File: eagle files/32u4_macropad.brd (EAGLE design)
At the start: 75.2 x 98.6 mm, 89 parts, among them IC1 IS31FL3733-TQLS4, J1 TYPE-C-31-M-12, Q1 16Mhz, SW2 SWITCH-SMD-EVP-BB2A9B00, U1 ATMEGA32U4-TQFP44

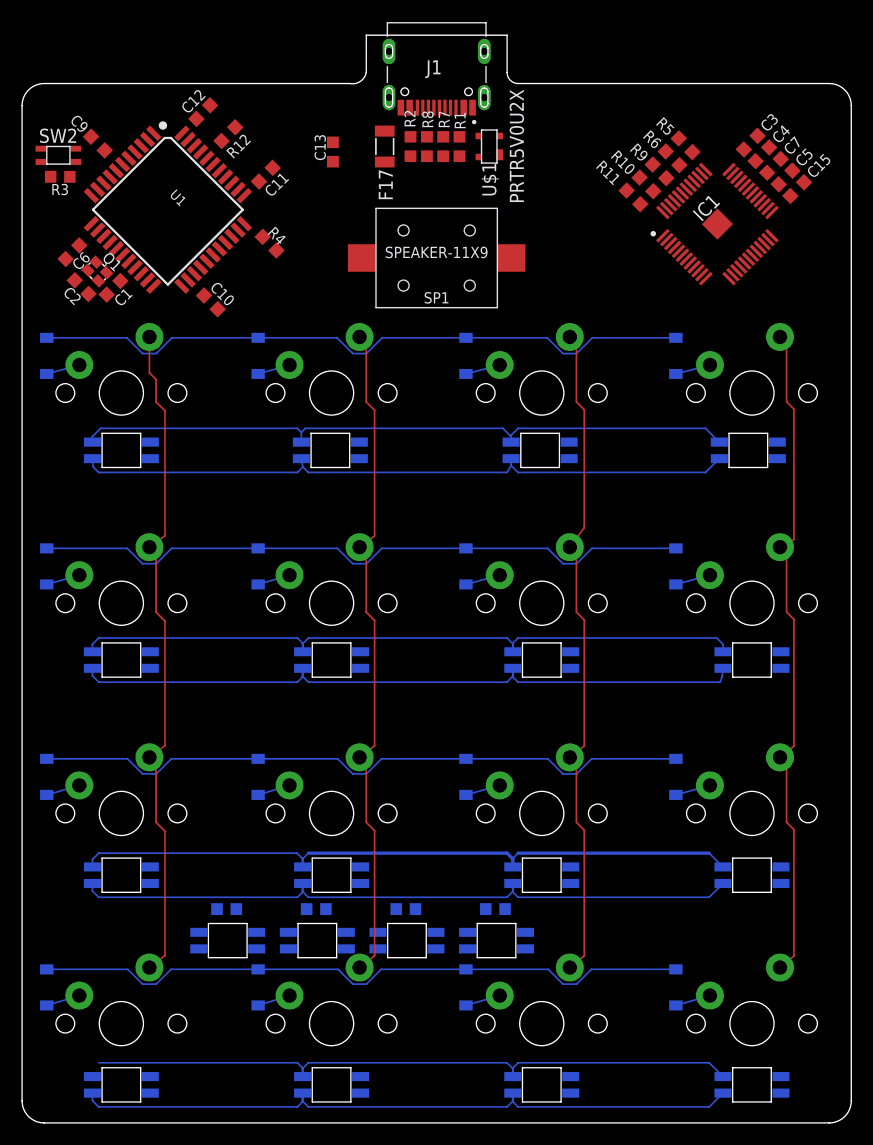
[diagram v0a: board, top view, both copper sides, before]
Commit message: ESD Finished, led driver work, board placement work
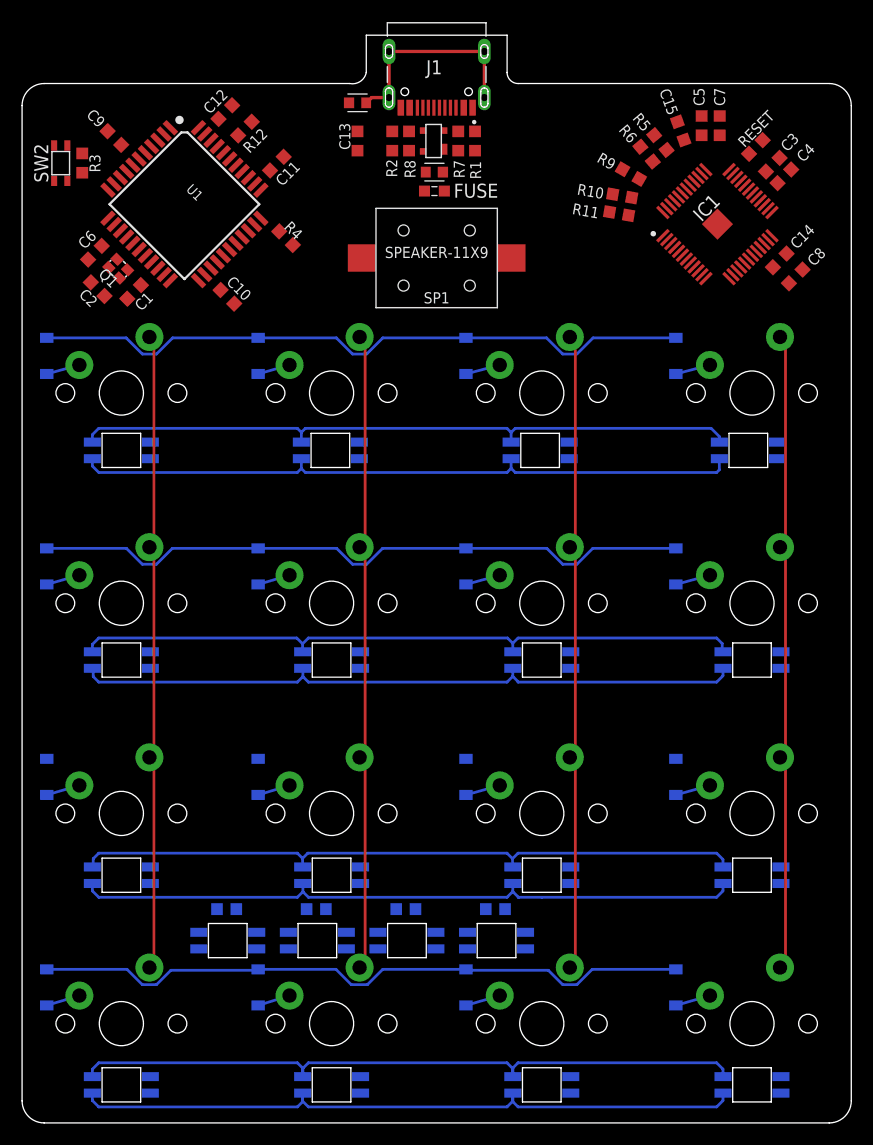
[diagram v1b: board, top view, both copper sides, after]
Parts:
- removed F17: 1206L012, polyfuse-smd_10:1206L
- added C14: 0.1uF, Components:C0603
- added C8: 0.47uF, Components:C0603
- added FB1, FB2: FERRITE_BEAD, Filter:BEADC1608X95N
- added FUSE: 0603L050, polyfuse-smd_20:0603L
- added RESET: 20k, Components:R0603
- moved C15 11.8 mm to (69.7, 100.0), turned to 290 degrees
- moved C5 8.93 mm to (71.6, 100.4), turned to 270 degrees
- moved C7 6.12 mm to (73.3, 100.4), turned to 270 degrees
- moved U$1 5.07 mm to (47.3, 99.0)
- moved C3 2.83 mm to (78.1, 96.9), turned to 225 degrees
- moved C4 2.83 mm to (79.1, 95.8), turned to 225 degrees
- moved R9 2.60 mm to (65.2, 96.0), turned to 150 degrees
- moved C13 2.44 mm to (40.5, 99.0)
- moved R10 2.44 mm to (64.4, 94.1), turned to 170 degrees
- moved R6 2.38 mm to (66.6, 97.8), turned to 130 degrees
- moved R3 2.35 mm to (15.5, 97.0), turned to 270 degrees
- moved R5 2.30 mm to (67.9, 98.9), turned to 130 degrees
- moved C6 2.04 mm to (16.7, 88.9)
- moved C12 2.00 mm to (28.5, 101.7)
- moved R11 1.97 mm to (64.2, 92.5), turned to 350 degrees
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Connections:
- net INTBUSE?? renamed INTBUSE
- removed net N$27: R8.2, U1.3
- new net 1: C14.1, C8.1
- new net N$14: J1.B6, R8.1
- new net N$16: J1.B7, R7.1
- new net N$18: R8.2
- new net N$19: R7.2
- new net N$22: FB2.1, J1.S1, J1.S2, J1.S3, J1.S4
- new net N$24: FB1.2, FUSE.2
- new net VCC1: C14.2, C8.2, IC1.20
- net 0: now also FB2.2, IC1.43, IC1.44, RESET.2; no longer J1.S1, J1.S2, J1.S3, J1.S4
- net AUDIO: now also U1.30; no longer U1.12
- net D+: now also U1.4; no longer J1.B6, R8.1
- net D-: now also U1.3; no longer J1.B7, R7.1
- net N$26: now also IC1.35, RESET.1; no longer R7.2, U1.4
- net VCC: now also FUSE.1; no longer F17.1, IC1.20
- net VUSB: now also FB1.1; no longer F17.2
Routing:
- net R2SWTCH: track 60.4 -> 0.00 mm
- net N$22: track 0.00 -> 19.3 mm
- net C0SWTCH: track 61.0 -> 58.2 mm
- net C1SWTCH: track 60.8 -> 58.4 mm
- net C3SWTCH: track 60.7 -> 58.4 mm
- net C2SWTCH: track 60.5 -> 58.4 mm
- net R3BLUE: track 60.9 -> 62.8 mm
- net R1RED: track 62.9 -> 61.3 mm
- net R1BLUE: track 62.8 -> 61.3 mm
- net R2BLUE: track 62.4 -> 61.3 mm
- net R2RED: track 62.4 -> 61.4 mm
- net R0RED: track 60.6 -> 61.2 mm

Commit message: Led driver finished, usb footprint made unilateral and fixed D+ D- connection, board work
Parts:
- removed R10, R9: 100k, Components:R0603
- R5, R6: value 1k -> 4.7k
- moved UGLOW1 110.1 mm to (-2.58, 121.5), turned to 270 degrees
- moved C21 109.0 mm to (-5.43, 121.5), turned to 270 degrees
- moved UGLOW2 99.0 mm to (-2.58, 113.4), turned to 270 degrees
- moved C20 97.8 mm to (-5.43, 113.3), turned to 270 degrees
- moved UGLOW3 88.0 mm to (-2.58, 105.3), turned to 270 degrees
- moved C19 86.7 mm to (-5.43, 105.2), turned to 270 degrees
- moved UGLOW4 77.2 mm to (-2.58, 97.2), turned to 270 degrees
- moved C18 75.7 mm to (-5.43, 97.1), turned to 270 degrees
- moved FB1 5.00 mm to (47.4, 91.2)
- moved FUSE 5.00 mm to (47.4, 89.5)
- moved U$1 5.00 mm to (47.3, 94.0), turned to 270 degrees
- moved R6 3.23 mm to (67.9, 94.9), turned to 135.9 degrees
- moved R5 3.08 mm to (69.1, 96.1), turned to 135 degrees
- moved R11 2.85 mm to (66.7, 93.7), turned to 135 degrees
- moved C5 2.84 mm to (74.1, 99.1), turned to 315 degrees
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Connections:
- removed net INTBUSE: IC1.45, R9.1
- removed net N$16: J1.B7, R7.1
- removed net N$19: R7.2
- net 0: no longer R10.2
- net D+: now also R8.2; no longer J1.A6
- net D-: now also R7.2; no longer J1.A7
- net N$14: now also J1.A7, J1.B7, R7.1; no longer J1.B6, R8.1
- net N$18: now also J1.A6, J1.B6, R8.1; no longer R8.2
- net SDB: no longer IC1.46, R10.1
- net VCC: now also IC1.46; no longer R9.2
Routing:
- net R3GREEN: track 0.00 -> 72.2 mm, vias 0 -> 4
- net VCC: track 0.00 -> 68.3 mm
- net R0GREEN: track 0.00 -> 57.6 mm, vias 0 -> 6
- net R0RED: track 61.2 -> 91.8 mm, vias 0 -> 1
- net R0BLUE: track 60.9 -> 81.2 mm, vias 0 -> 1
- net D+: track 0.00 -> 7.46 mm
- net D-: track 0.00 -> 6.20 mm
- net N$15: track 0.00 -> 5.59 mm
- net N$2: track 0.00 -> 5.57 mm
- net N$20: track 0.00 -> 2.41 mm
- net N$8: track 0.00 -> 2.38 mm
- net N$14: track 0.00 -> 2.27 mm
- net N$18: track 0.00 -> 2.25 mm
- net UNDGLOW: track 0.00 -> 2.12 mm

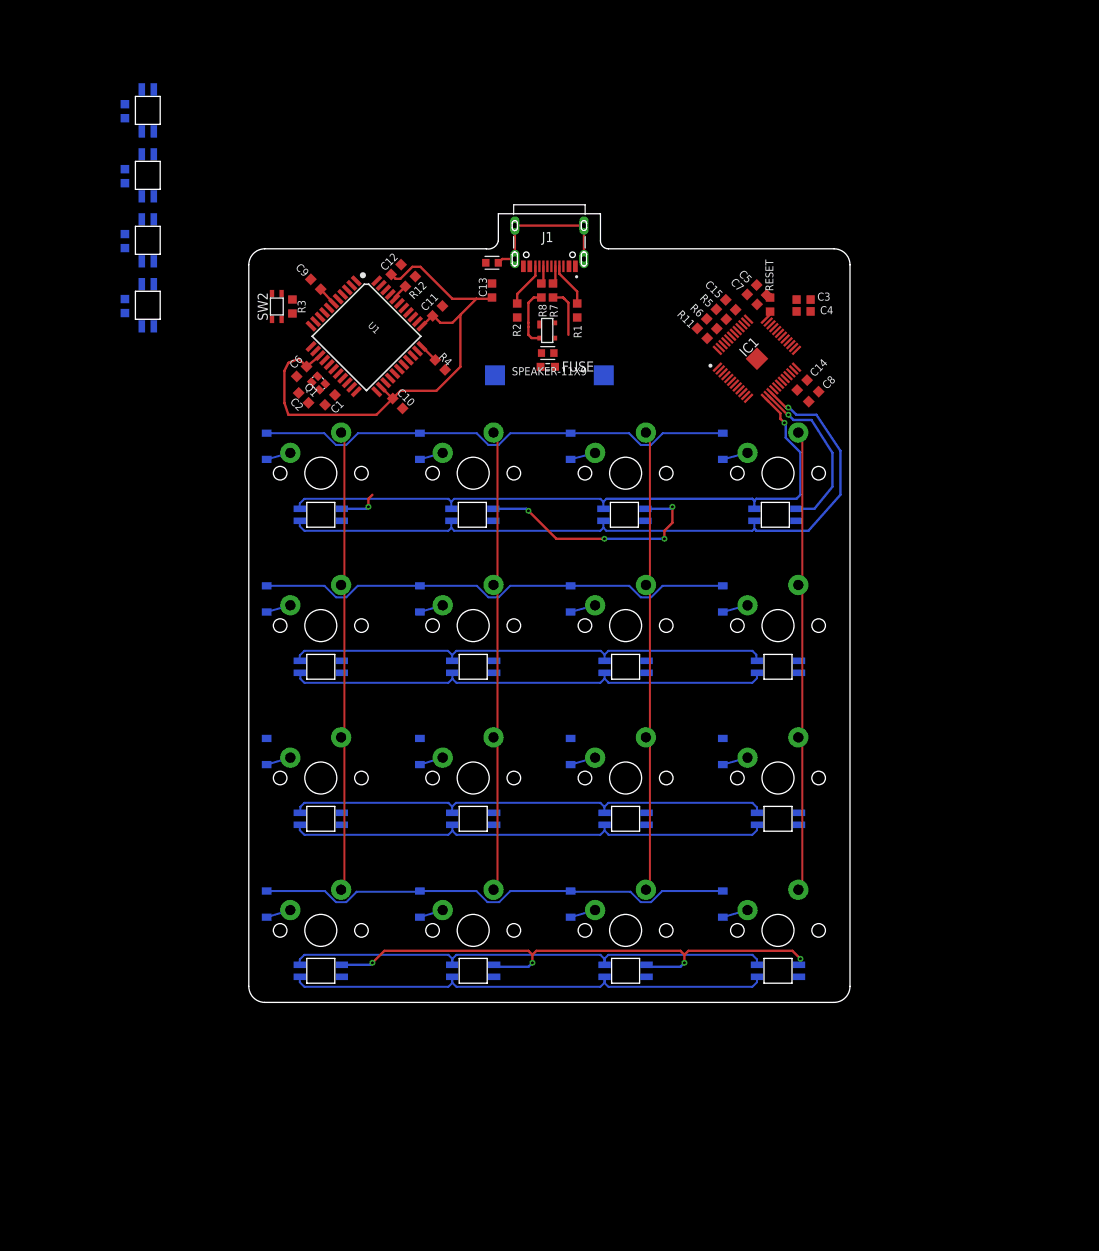
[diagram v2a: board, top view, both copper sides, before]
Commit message: Major board routing, GND net fix
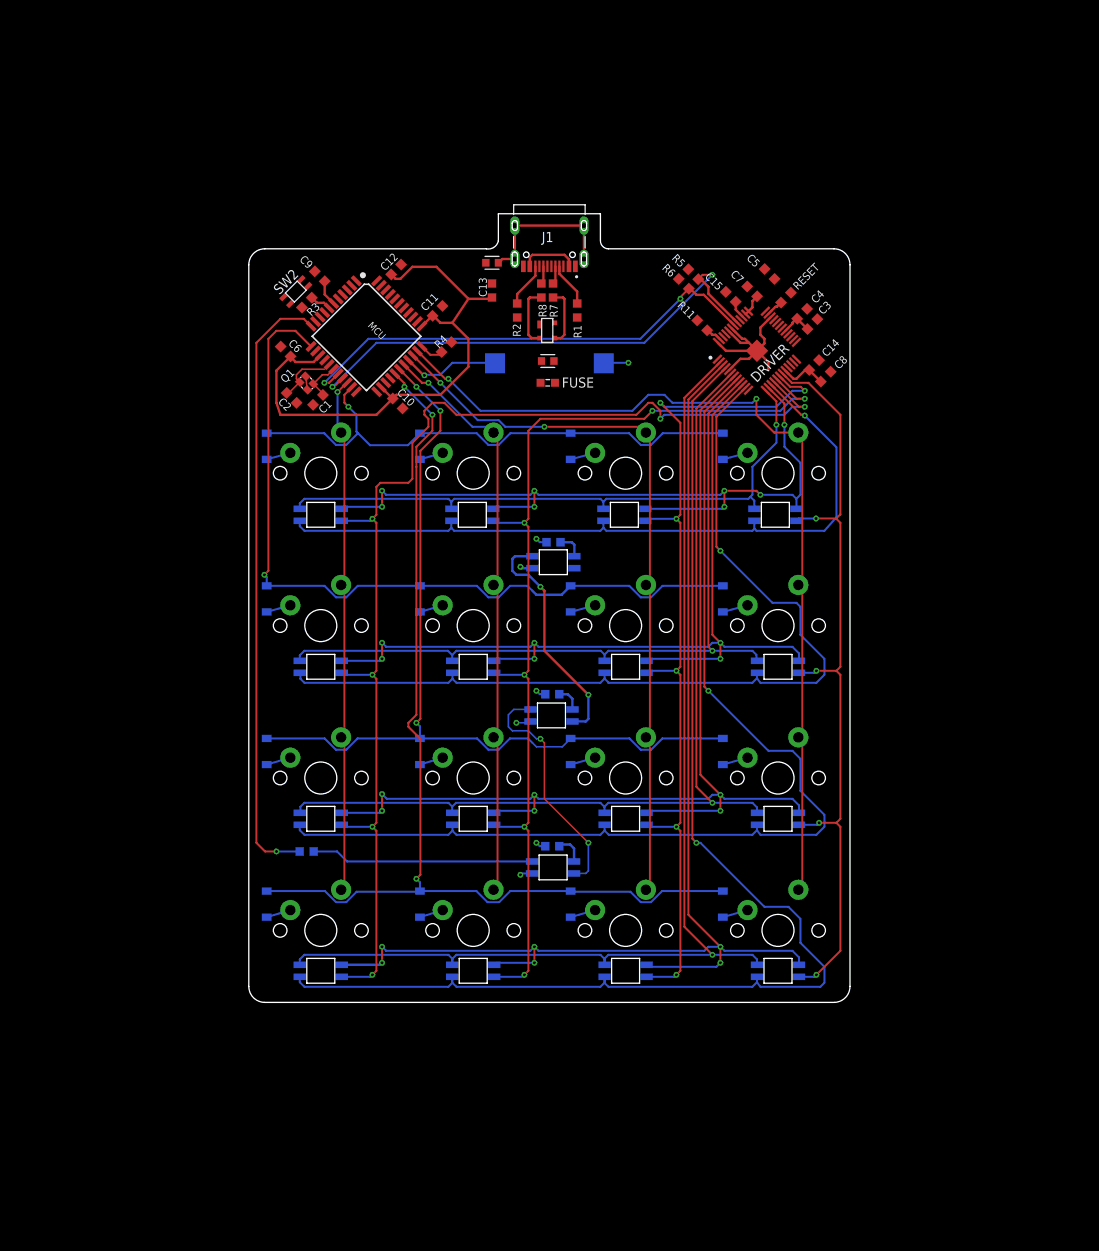
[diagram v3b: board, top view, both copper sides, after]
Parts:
- removed C18: 100uF, Components:C0603
- removed IC1: IS31FL3733-TQLS4, IS31FL3733-TQLS4:QFP50P900X900X120-49N
- removed UGLOW4: SK6812MINI-E, SK6812MINI-E:SK6812MINI-E
- added DRIVER: IS31FL3733-TQLS4, IS31FL3733-TQLS4:QFP50P900X900X120-49N
- moved UGLOW1 107.3 mm to (48.1, 26.9), turned to 0 degrees
- moved C21 106.3 mm to (48.0, 29.6), turned to 180 degrees
- moved UGLOW2 84.3 mm to (47.9, 45.9), turned to 0 degrees
- moved C20 83.9 mm to (48.0, 48.6), turned to 180 degrees
- moved R12 72.4 mm to (17.3, 28.9), flipped to the bottom, turned to 0 degrees
- moved C19 65.5 mm to (48.1, 67.6), turned to 180 degrees
- moved UGLOW3 64.7 mm to (48.1, 65.1), turned to 0 degrees
- moved R5 6.10 mm to (65.6, 101.1)
- moved R6 6.10 mm to (64.4, 99.9)
- moved C3 3.26 mm to (80.5, 94.8), turned to 225 degrees
- moved C6 3.20 mm to (14.7, 91.4), turned to 135 degrees
- moved SW2 3.02 mm to (15.9, 98.9), turned to 225 degrees
- moved C14 2.92 mm to (80.7, 89.7)
- moved C8 2.92 mm to (82.2, 88.3)
- moved R4 2.38 mm to (34.8, 92.0), turned to 225 degrees
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- renumbered U1 to MCU
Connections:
- removed net 0: C1.1, C10.2, C11.2, C12.2, C13.2, C15.1, C18.1, C19.1, C2.1, C20.1, C21.1, C3.1, C4.1, C5.1, C6.2, C7.1, C9.1, FB2.2, IC1.12, IC1.34, IC1.43, IC1.44, IC1.48, IC1.49, IC1.5, J1.A1B12, J1.B1A12, MCU.15, MCU.23, MCU.35, MCU.43, MCU.5, Q1.2, Q1.4, R1.1, R11.1, R2.1, R4.1, RESET.2, SP1.-, SW2.A@1, SW2.A@2, U$1.1, UGLOW1.P$3, UGLOW2.P$3, UGLOW3.P$3, UGLOW4.P$3
- removed net 1: C14.1, C8.1
- removed net N$6: UGLOW3.P$2, UGLOW4.P$4
- removed net SDB: MCU.41
- new net GND: C1.1, C10.2, C11.2, C12.2, C13.2, C14.1, C15.1, C19.1, C2.1, C20.1, C21.1, C3.1, C4.1, C5.1, C6.2, C7.1, C8.1, C9.1, DRIVER.12, DRIVER.34, DRIVER.43, DRIVER.44, DRIVER.48, DRIVER.49, DRIVER.5, FB2.2, J1.A1B12, J1.B1A12, MCU.15, MCU.23, MCU.35, MCU.43, MCU.5, Q1.2, Q1.4, R1.1, R11.1, R2.1, R4.1, RESET.2, SW2.A@1, SW2.A@2, U$1.1, UGLOW1.P$3, UGLOW2.P$3, UGLOW3.P$3
- new net N$40: SP1.-
- net C0RGB: now also DRIVER.16; no longer IC1.16
- net C0SWTCH: now also MCU.20; no longer MCU.21
- net C1RGB: now also DRIVER.17; no longer IC1.17
- net C1SWTCH: now also MCU.29; no longer MCU.25
- net C2RGB: now also DRIVER.18; no longer IC1.18
- net C3RGB: now also DRIVER.19; no longer IC1.19
- net N$10: now also DRIVER.47; no longer IC1.47
- net N$26: now also DRIVER.35; no longer IC1.35
- net R0BLUE: now also DRIVER.13; no longer IC1.13
- net R0GREEN: now also DRIVER.14; no longer IC1.14
- net R0RED: now also DRIVER.15; no longer IC1.15
- net R0SWTCH: now also MCU.21; no longer MCU.20
- net R1BLUE: now also DRIVER.9; no longer IC1.9
- net R1GREEN: now also DRIVER.10; no longer IC1.10
- net R1RED: now also DRIVER.11; no longer IC1.11
- net R1SWTCH: now also MCU.12; no longer MCU.22
- net R2BLUE: now also DRIVER.6; no longer IC1.6
- net R2GREEN: now also DRIVER.7; no longer IC1.7
- net R2RED: now also DRIVER.8; no longer IC1.8
- net R2SWTCH: now also MCU.28; no longer MCU.26
- net R3BLUE: now also DRIVER.2; no longer IC1.2
- net R3GREEN: now also DRIVER.3; no longer IC1.3
- net R3RED: now also DRIVER.4; no longer IC1.4
- net SCL: now also DRIVER.42; no longer IC1.42
- net SDA: now also DRIVER.41; no longer IC1.41
- net UNDGLOW: now also MCU.11; no longer MCU.40
- net VCC: now also DRIVER.29, DRIVER.37, DRIVER.38, DRIVER.39, DRIVER.46; no longer C18.2, IC1.29, IC1.37, IC1.38, IC1.39, IC1.46, UGLOW4.P$1
- net VCC1: now also DRIVER.20; no longer IC1.20
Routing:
- net C0RGB: track 0.00 -> 149.0 mm, vias 0 -> 6
- net R2GREEN: track 0.00 -> 135.3 mm, vias 0 -> 6
- net C1RGB: track 0.00 -> 125.9 mm, vias 0 -> 6
- net R1GREEN: track 0.00 -> 114.3 mm, vias 0 -> 6
- net C2RGB: track 0.00 -> 112.4 mm, vias 0 -> 6
- net R2SWTCH: track 0.00 -> 111.1 mm, vias 0 -> 3
- net C3RGB: track 0.00 -> 98.6 mm, vias 0 -> 4
- net R3RED: track 62.8 -> 159.2 mm, vias 0 -> 1
- net R3GREEN: track 72.2 -> 156.4 mm, vias 4 -> 6
- net R3BLUE: track 62.8 -> 140.2 mm, vias 0 -> 1
- net R2RED: track 61.4 -> 136.1 mm, vias 0 -> 1
- net UNDGLOW: track 2.12 -> 76.8 mm, vias 0 -> 1
- net R3SWTCH: track 60.5 -> 129.3 mm, vias 0 -> 3
- net SDA: track 0.00 -> 64.6 mm, vias 0 -> 2
- net SCL: track 0.00 -> 60.4 mm, vias 0 -> 2
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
